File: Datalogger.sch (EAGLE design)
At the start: 6 parts, among them IC1 7805T

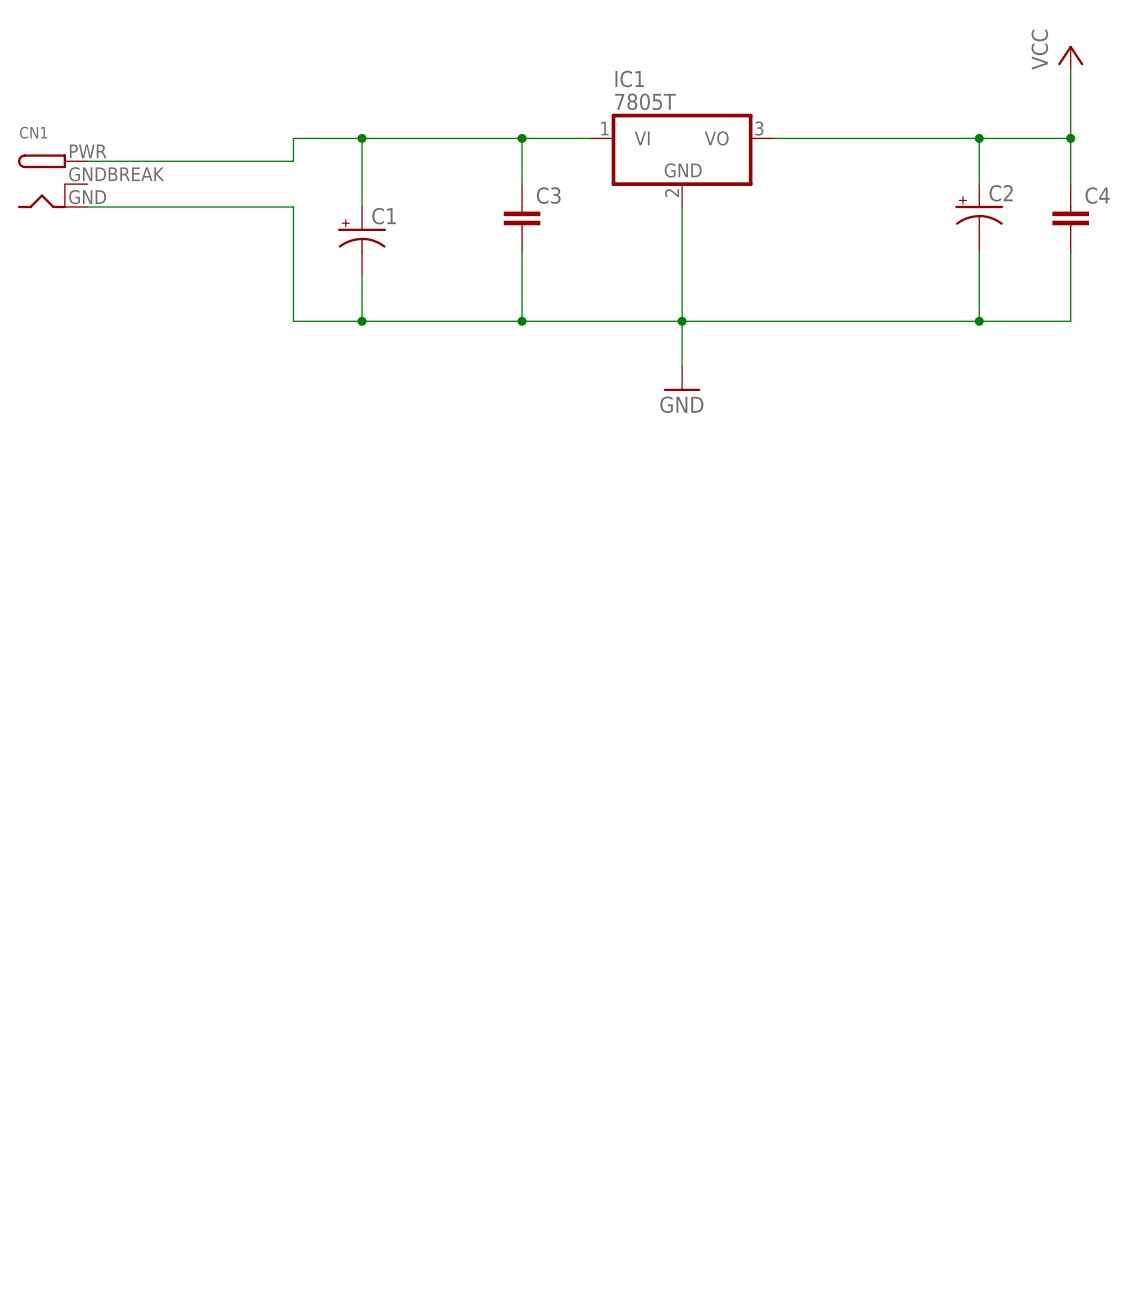
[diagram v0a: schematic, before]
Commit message: microcontroller subcircuit completed
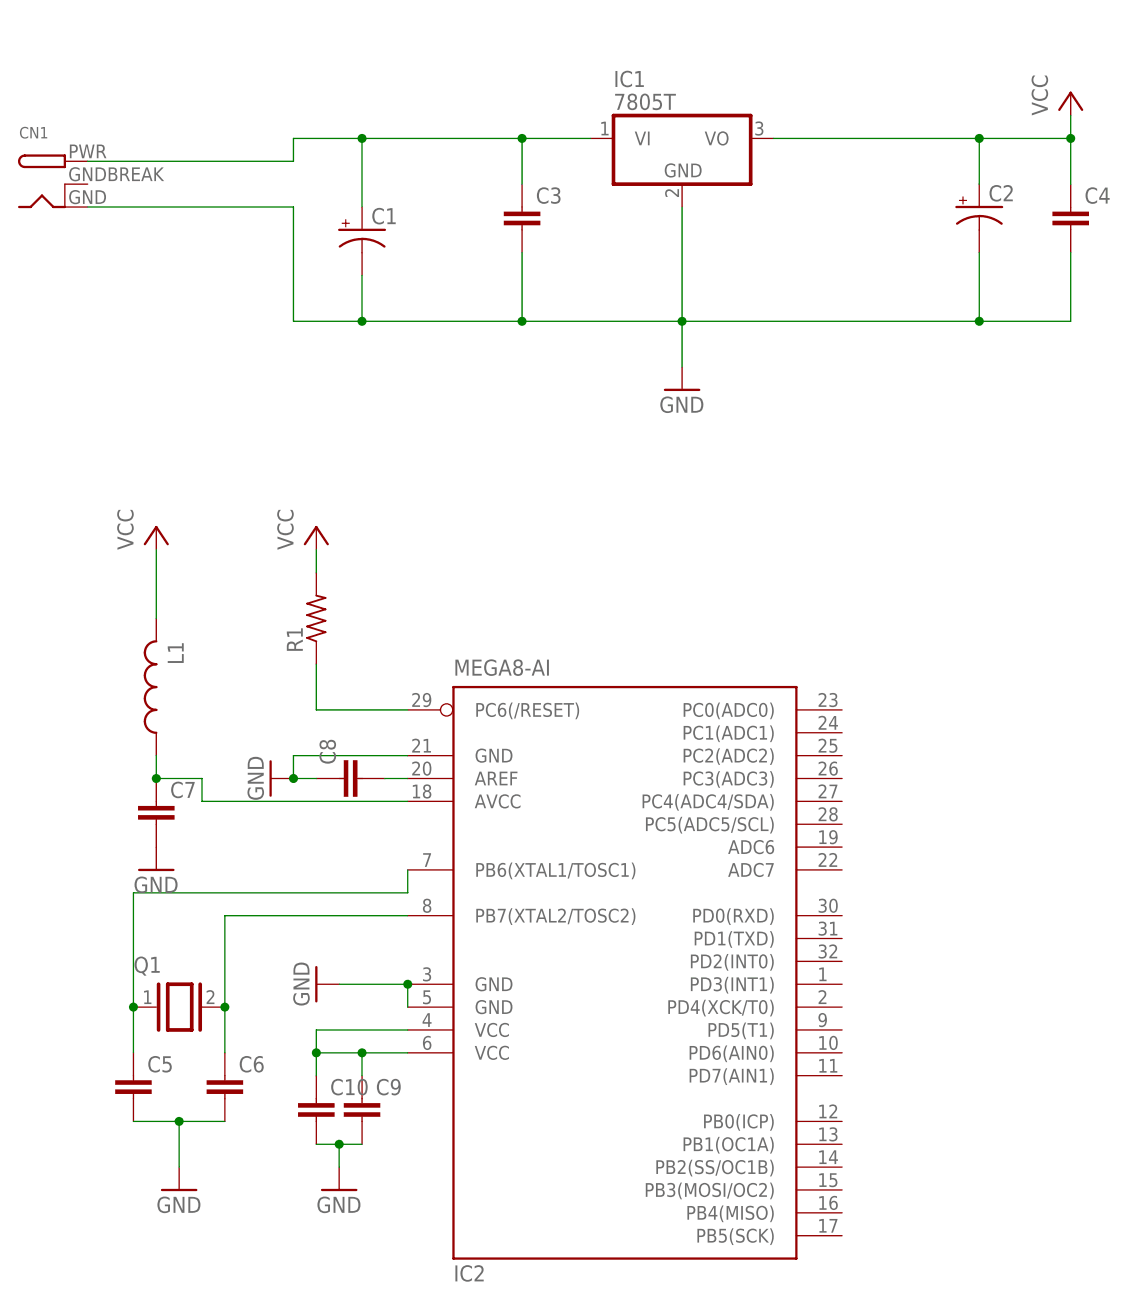
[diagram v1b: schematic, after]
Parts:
- added C10, C5, C6, C7, C8, C9: (no value), rcl:C-EUC0603
- added IC2: MEGA8-AI, atmel:MEGA8-AI
- added L1: (no value), rcl:L-USL2012C
- added Q1: (no value), special:XTAL/S
- added R1: (no value), rcl:R-US_R0603
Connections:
- new net N$2: IC2.PC6(/RESET), R1.1
- new net N$3: C6.1, IC2.PB7(XTAL2/TOSC2), Q1.2
- new net N$4: C5.1, IC2.PB6(XTAL1/TOSC1), Q1.1
- new net N$5: C7.1, IC2.AVCC, L1.1
- new net N$6: C10.1, C9.1, IC2.VCC@1, IC2.VCC@2
- new net N$7: C8.2, IC2.AREF
- net GND: now also C10.2, C5.2, C6.2, C7.2, C8.1, C9.2, IC2.GND, IC2.GND@1, IC2.GND@2
- net VCC: now also L1.2, R1.2

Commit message: pcb design started
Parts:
- added BAT1: BATTERY_1236_C, Itead_BP_110825.lbr:BATTERY_1236_C
- added C11, C12, C13, C14, C15: 100nF, rcl:C-EUC0603
- added R2, R3: 2.2k, adafruit:R-US_R0603
- added U1: DS1307Z, SparkFun-Clocks:DS1307Z
- added X1: 32.768KHZ, adafruit:XTAL-3.2X1.5
- added X2, X3, X4, X5: (no value), con-ptr500:AK500/3
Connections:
- new net A0: IC2.PC0(ADC0), X2-1.KL
- new net A1: IC2.PC1(ADC1), X3-1.KL
- new net A2: IC2.PC2(ADC2), X4-1.KL
- new net A3: IC2.PC3(ADC3), X5-1.KL
- new net N$10: U1.X2, X1.P$1
- new net N$8: BAT1.+, U1.VBATT
- new net N$9: U1.X1, X1.P$2
- new net SCL: IC2.PC5(ADC5/SCL), R3.2, U1.SCL
- new net SDA: IC2.PC4(ADC4/SDA), R2.1, U1.SDA
- new net SQW: U1.SQW
- net GND: now also BAT1.-, C11.1, C12.1, C13.1, C14.1, C15.1, U1.GND, X2-2.KL, X3-2.KL, X4-2.KL, X5-2.KL
- net VCC: now also C11.2, C12.2, C13.2, C14.2, C15.2, R2.2, R3.1, U1.VCC, X2-3.KL, X3-3.KL, X4-3.KL, X5-3.KL
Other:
- note added: "RTC"
